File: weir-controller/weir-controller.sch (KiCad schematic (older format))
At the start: 48 parts, among them J1 Screw_Terminal_01x02, J2 Screw_Terminal_01x04, J3 Screw_Terminal_01x04, J4 USB_B_Mini, J5 Wurth_74980104400, J6 Screw_Terminal_01x02, Q1 PSMN0R7-25YLD, Q2 PSMN0R7-25YLD, Q3 PSMN0R7-25YLD, Q4 PSMN0R7-25YLD, SW1 SW_Push, U1 ESP32-WROOM-32U, U2 DP83825IRMQR, U3 CP2102N-A01-GQFN24, U4 TL1963A-33DCYR

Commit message: Try 4 layer for RMII trace impedance
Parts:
- D1: symbol custom-parts:LED_ABGR -> Custom:LED_ABGR
- J4: footprint custom-parts:54819-0589 -> Custom:54819-0589
- J5: footprint custom-parts:Wurth_74980104400 -> Custom:Wurth_74980104400; symbol custom-parts:Wurth_74980104400 -> Custom:Wurth_74980104400
- SW1: footprint custom-parts:PTS636 -> Custom:PTS636
- U1: footprint custom-parts:ESP32-WROOM-32U -> Custom:ESP32-WROOM-32U
- U2: footprint custom-parts:TI_RMQ0024A -> Custom:TI_RMQ0024A; symbol custom-parts:DP83825IRMQR -> Custom:DP83825IRMQR
- U4: symbol custom-parts:TL1963A-33DCYR -> Custom:TL1963A-33DCYR
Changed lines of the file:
@@
 F 0 "U1" H 2500 4981 50  0000 C CNN
 F 1 "ESP32-WROOM-32U" H 2500 4890 50  0000 C CNN
-F 2 "custom-parts:ESP32-WROOM-32U" H 2500 1900 50  0001 C CNN
+F 2 "Custom:ESP32-WROOM-32U" H 2500 1900 50  0001 C CNN
 F 3 "https://www.espressif.com/sites/default/files/documentation/esp32-wroom-32d_esp32-wroom-32u_datasheet_en.pdf" H 2200 3450 50  0001 C CNN
 	1    2500 3400
@@
 F 0 "J4" H 8657 8517 50  0000 C CNN
 F 1 "USB_B_Mini" H 8657 8426 50  0000 C CNN
-F 2 "custom-parts:54819-0589" H 8750 8000 50  0001 C CNN
+F 2 "Custom:54819-0589" H 8750 8000 50  0001 C CNN
 F 3 "~" H 8750 8000 50  0001 C CNN
 	1    8600 8050
@@
 $EndComp
 $Comp
-L custom-parts:Wurth_74980104400 J5
+L Custom:Wurth_74980104400 J5
 U 1 1 5E9BA03E
 P 9900 3100
 F 0 "J5" H 10392 4448 50  0000 C CNN
 F 1 "Wurth_74980104400" H 10392 4357 50  0000 C CNN
-F 2 "custom-parts:Wurth_74980104400" H 10475 2675 50  0001 C CNN
+F 2 "Custom:Wurth_74980104400" H 10475 2675 50  0001 C CNN
 F 3 "" H 11375 3825 50  0001 C CNN
 	1    9900 3100
@@
 	3100 2700 3200 2700
 $Comp
-L custom-parts:DP83825IRMQR U2
+L Custom:DP83825IRMQR U2
 U 1 1 5E9C7073
 P 7400 2800
 F 0 "U2" H 7400 1611 50  0000 C CNN
 F 1 "DP83825IRMQR" H 7400 1520 50  0000 C CNN
-F 2 "custom-parts:TI_RMQ0024A" H 7350 1400 50  0001 C CNN
+F 2 "Custom:TI_RMQ0024A" H 7350 1400 50  0001 C CNN
 F 3 "" H 7100 3100 50  0001 C CNN
 	1    7400 2800
@@
 USB_N
 $Comp
-L custom-parts:TL1963A-33DCYR U4
+L Custom:TL1963A-33DCYR U4
 U 1 1 5EBD715B
 P 13000 2550
@@
 F 0 "SW1" H 3750 5185 50  0000 C CNN
 F 1 "SW_Push" H 3750 5094 50  0000 C CNN
-F 2 "custom-parts:PTS636" H 3750 5100 50  0001 C CNN
+F 2 "Custom:PTS636" H 3750 5100 50  0001 C CNN
 F 3 "~" H 3750 5100 50  0001 C CNN
 	1    3750 4900
@@
 FACTORY_RESET
 $Comp
-L custom-parts:LED_ABGR D1
+L Custom:LED_ABGR D1
 U 1 1 5ECC3E30
 P 3700 1650

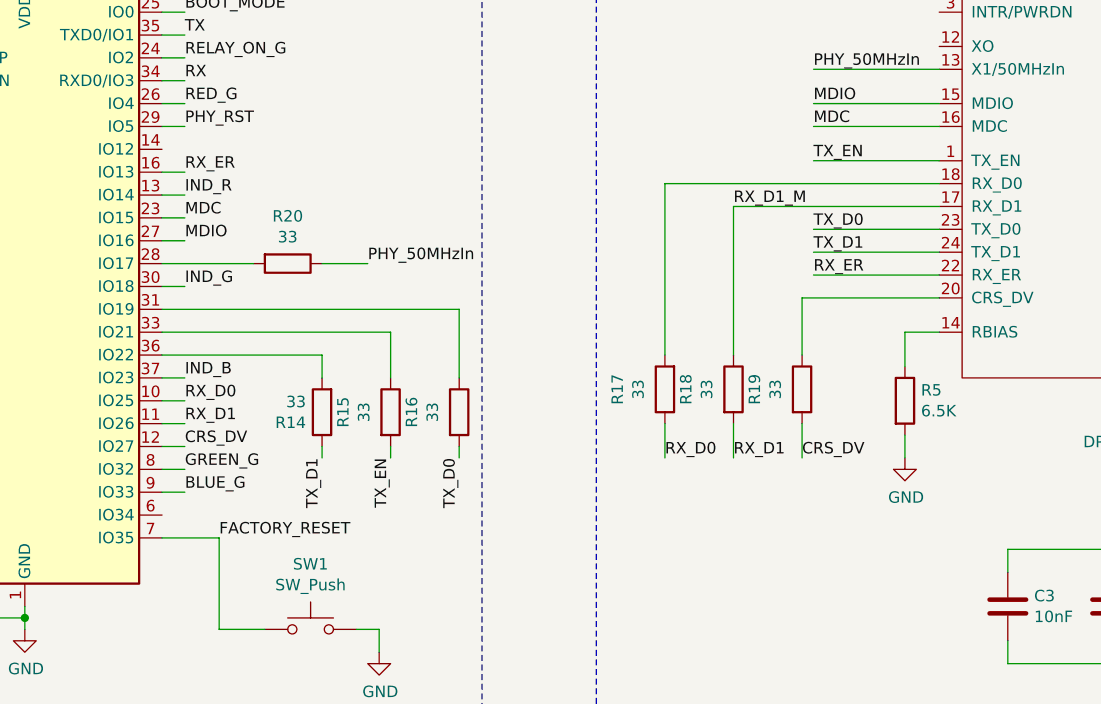
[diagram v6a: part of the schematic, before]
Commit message: Project Updates
Final ref of Weir Controller board. Starting Davis Receiver Board. The later only has the PoE power stage captured.
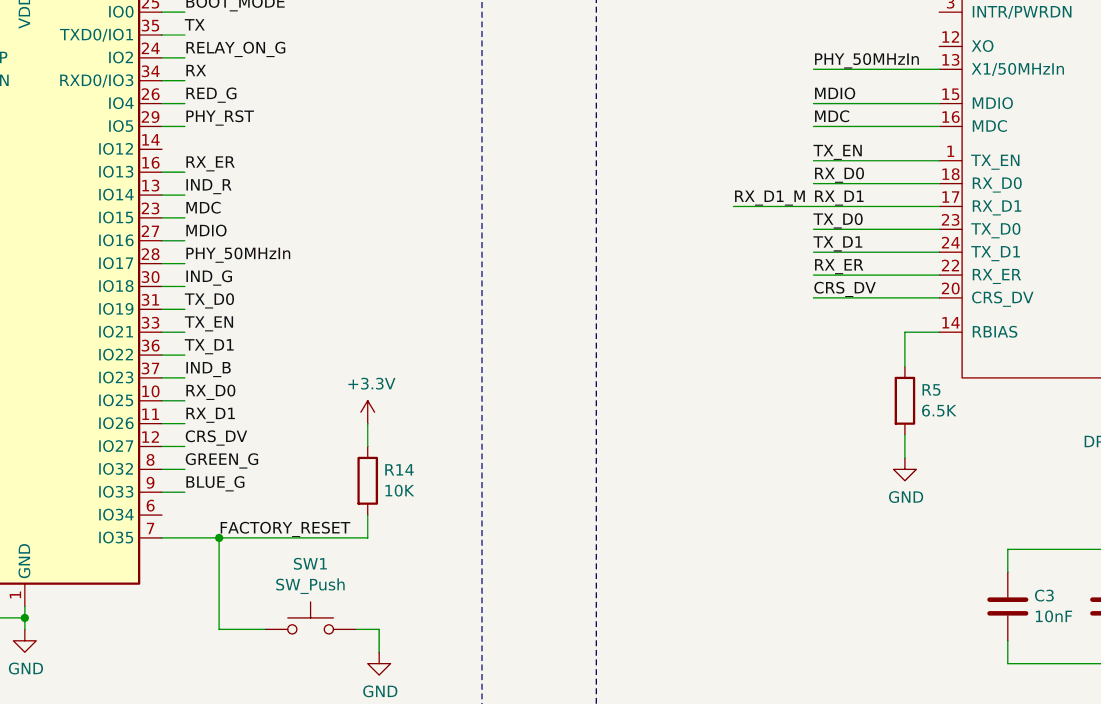
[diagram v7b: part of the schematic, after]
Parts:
- removed R15, R16, R17, R18, R19, R20: 33, Resistor_SMD:R_0805_2012Metric_Pad1.15x1.40mm_HandSolder, symbol Device:R
- R14: value 33 -> 10K; footprint Resistor_SMD:R_0805_2012Metric_Pad1.15x1.40mm_HandSolder -> Resistor_SMD:R_0805_2012Metric_Pad1.20x1.40mm_HandSolder
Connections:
- net RX_D1_M is gone; now on net RX_D1: R6.2, U2.17 (RX_D1)
- net +3V3: now also R14.1
- net CRS_DV: now also U2.20 (CRS_DV)
- net FACTORY_RESET: now also R14.2
- net PHY_50MHzIn: now also U1.28 (IO17)
- net RX_D0: now also U2.18 (RX_D0)
- net TX_D0: now also U1.31 (IO19)
- net TX_D1: now also U1.36 (IO22); no longer R14.1
- net TX_EN: now also U1.33 (IO21)
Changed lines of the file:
@@
 Text Label 5950 2850 0    50   ~ 0
 TX_EN
-Text Label 5300 4150 0    50   ~ 0
+Text Label 5950 2950 0    50   ~ 0
 RX_D0
-Text Label 5600 4150 0    50   ~ 0
+Text Label 5950 3050 0    50   ~ 0
 RX_D1
 Text Label 5950 3150 0    50   ~ 0
@@
 Text Label 5950 3350 0    50   ~ 0
 RX_ER
-Text Label 5900 4150 0    50   ~ 0
+Text Label 5950 3450 0    50   ~ 0
 CRS_DV
 Wire Wire Line
@@
 Wire Wire Line
 	5950 3350 6500 3350
-Text Label 4100 4150 3    50   ~ 0
+Text Label 3200 3600 0    50   ~ 0
 TX_EN
-Text Label 4400 4150 3    50   ~ 0
+Text Label 3200 3500 0    50   ~ 0
 TX_D0
-Text Label 3800 4150 3    50   ~ 0
+Text Label 3200 3700 0    50   ~ 0
 TX_D1
 Text Label 3200 3900 0    50   ~ 0
@@
 Text Label 3200 3100 0    50   ~ 0
 MDC
-Text Label 4000 3300 0    50   ~ 0
+Text Label 3200 3300 0    50   ~ 0
 PHY_50MHzIn
 Wire Wire Line
@@
 Text Label 2000 9000 0    50   ~ 0
 RELAY_NEGATIVE
-$Comp
-L Device:R R16
-U 1 1 5F2DDFD5
-P 4400 3950
-F 0 "R16" V 4193 3950 50  0000 C CNN
-F 1 "33" V 4284 3950 50  0000 C CNN
-F 2 "Resistor_SMD:R_0805_2012Metric_Pad1.15x1.40mm_HandSolder" V 4330 3950 50  0001 C CNN
-F 3 "~" H 4400 3950 50  0001 C CNN
-	1    4400 3950
-	1    0    0    -1
-$EndComp
-$Comp
-L Device:R R18
-U 1 1 5F2DF6D0
-P 5600 3850
-F 0 "R18" V 5393 3850 50  0000 C CNN
-F 1 "33" V 5484 3850 50  0000 C CNN
-F 2 "Resistor_SMD:R_0805_2012Metric_Pad1.15x1.40mm_HandSolder" V 5530 3850 50  0001 C CNN
-F 3 "~" H 5600 3850 50  0001 C CNN
-	1    5600 3850
-	1    0    0    -1
-$EndComp
-$Comp
-L Device:R R17
-U 1 1 5F2E0674
-P 5300 3850
-F 0 "R17" V 5507 3850 50  0000 C CNN
-F 1 "33" V 5416 3850 50  0000 C CNN
-F 2 "Resistor_SMD:R_0805_2012Metric_Pad1.15x1.40mm_HandSolder" V 5230 3850 50  0001 C CNN
-F 3 "~" H 5300 3850 50  0001 C CNN
-	1    5300 3850
-	-1   0    0    1
-$EndComp
-$Comp
-L Device:R R14
-U 1 1 5F2E2F76
-P 3800 3950
-F 0 "R14" H 3870 3996 50  0000 L CNN
-F 1 "33" H 3870 3905 50  0000 L CNN
-F 2 "Resistor_SMD:R_0805_2012Metric_Pad1.15x1.40mm_HandSolder" V 3730 3950 50  0001 C CNN
-F 3 "~" H 3800 3950 50  0001 C CNN
-	1    3800 3950
-	-1   0    0    1
-$EndComp
-$Comp
-L Device:R R19
-U 1 1 5F2E5EAA
-P 5900 3850
-F 0 "R19" V 5693 3850 50  0000 C CNN
-F 1 "33" V 5784 3850 50  0000 C CNN
-F 2 "Resistor_SMD:R_0805_2012Metric_Pad1.15x1.40mm_HandSolder" V 5830 3850 50  0001 C CNN
-F 3 "~" H 5900 3850 50  0001 C CNN
-	1    5900 3850
-	1    0    0    -1
-$EndComp
-Wire Wire Line
-	3800 3700 3800 3800
-Wire Wire Line
-	3100 3700 3800 3700
-Wire Wire Line
-	4100 3600 4100 3800
-Wire Wire Line
-	3100 3600 4100 3600
-Wire Wire Line
-	4400 3500 4400 3800
-Wire Wire Line
-	3100 3500 4400 3500
-Wire Wire Line
-	5300 2950 5300 3700
-Wire Wire Line
-	5300 2950 6500 2950
-Wire Wire Line
-	5600 3050 5600 3700
 Wire Wire Line
 	5600 3050 6500 3050
-Wire Wire Line
-	5900 3450 5900 3700
-Wire Wire Line
-	5900 3450 6500 3450
-Wire Wire Line
-	5300 4000 5300 4150
-Wire Wire Line
-	5600 4000 5600 4150
-Wire Wire Line
-	5900 4000 5900 4150
-Wire Wire Line
-	4400 4100 4400 4150
-Wire Wire Line
-	4100 4100 4100 4150
-Wire Wire Line
-	3800 4100 3800 4150
-$Comp
-L Device:R R15
-U 1 1 5F2DBDD5
-P 4100 3950
-F 0 "R15" V 3893 3950 50  0000 C CNN
-F 1 "33" V 3984 3950 50  0000 C CNN
-F 2 "Resistor_SMD:R_0805_2012Metric_Pad1.15x1.40mm_HandSolder" V 4030 3950 50  0001 C CNN
-F 3 "~" H 4100 3950 50  0001 C CNN
-	1    4100 3950
-	1    0    0    -1
-$EndComp
 Text Label 5600 3050 0    50   ~ 0
 RX_D1_M
-$Comp
-L Device:R R20
-U 1 1 5F5E6B7B
-P 3650 3300
-F 0 "R20" V 3443 3300 50  0000 C CNN
-F 1 "33" V 3534 3300 50  0000 C CNN
-F 2 "Resistor_SMD:R_0805_2012Metric_Pad1.15x1.40mm_HandSolder" V 3580 3300 50  0001 C CNN
-F 3 "~" H 3650 3300 50  0001 C CNN
-	1    3650 3300
-	0    1    1    0
-$EndComp
-Wire Wire Line
-	3100 3300 3500 3300
-Wire Wire Line
-	3800 3300 4000 3300
+Wire Wire Line
+	3100 3500 3200 3500
+Wire Wire Line
+	3100 3600 3200 3600
+Wire Wire Line
+	3100 3700 3200 3700
+Wire Wire Line
+	5950 2950 6500 2950
+Wire Wire Line
+	5950 3450 6500 3450
+Wire Wire Line
+	3100 3300 3200 3300
+$Comp
+L Device:R R14
+U 1 1 605FF3A8
+P 4000 4250
+F 0 "R14" H 4070 4296 50  0000 L CNN
+F 1 "10K" H 4070 4205 50  0000 L CNN
+F 2 "Resistor_SMD:R_0805_2012Metric_Pad1.20x1.40mm_HandSolder" V 3930 4250 50  0001 C CNN
+F 3 "~" H 4000 4250 50  0001 C CNN
+	1    4000 4250
+	1    0    0    -1
+$EndComp
+Wire Wire Line
+	3350 4500 4000 4500
+Wire Wire Line
+	4000 4500 4000 4400
+Connection ~ 3350 4500
+$Comp
+L power:+3.3V #PWR029
+U 1 1 606137F9
+P 4000 4000
+F 0 "#PWR029" H 4000 3850 50  0001 C CNN
+F 1 "+3.3V" H 4015 4173 50  0000 C CNN
+F 2 "" H 4000 4000 50  0001 C CNN
+F 3 "" H 4000 4000 50  0001 C CNN
+	1    4000 4000
+	1    0    0    -1
+$EndComp
+Wire Wire Line
+	4000 4000 4000 4100
 $EndSCHEMATC
